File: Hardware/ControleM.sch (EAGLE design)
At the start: 17 parts, among them IC1 TL082P, IC2 TL082P, U1 LT1054CP

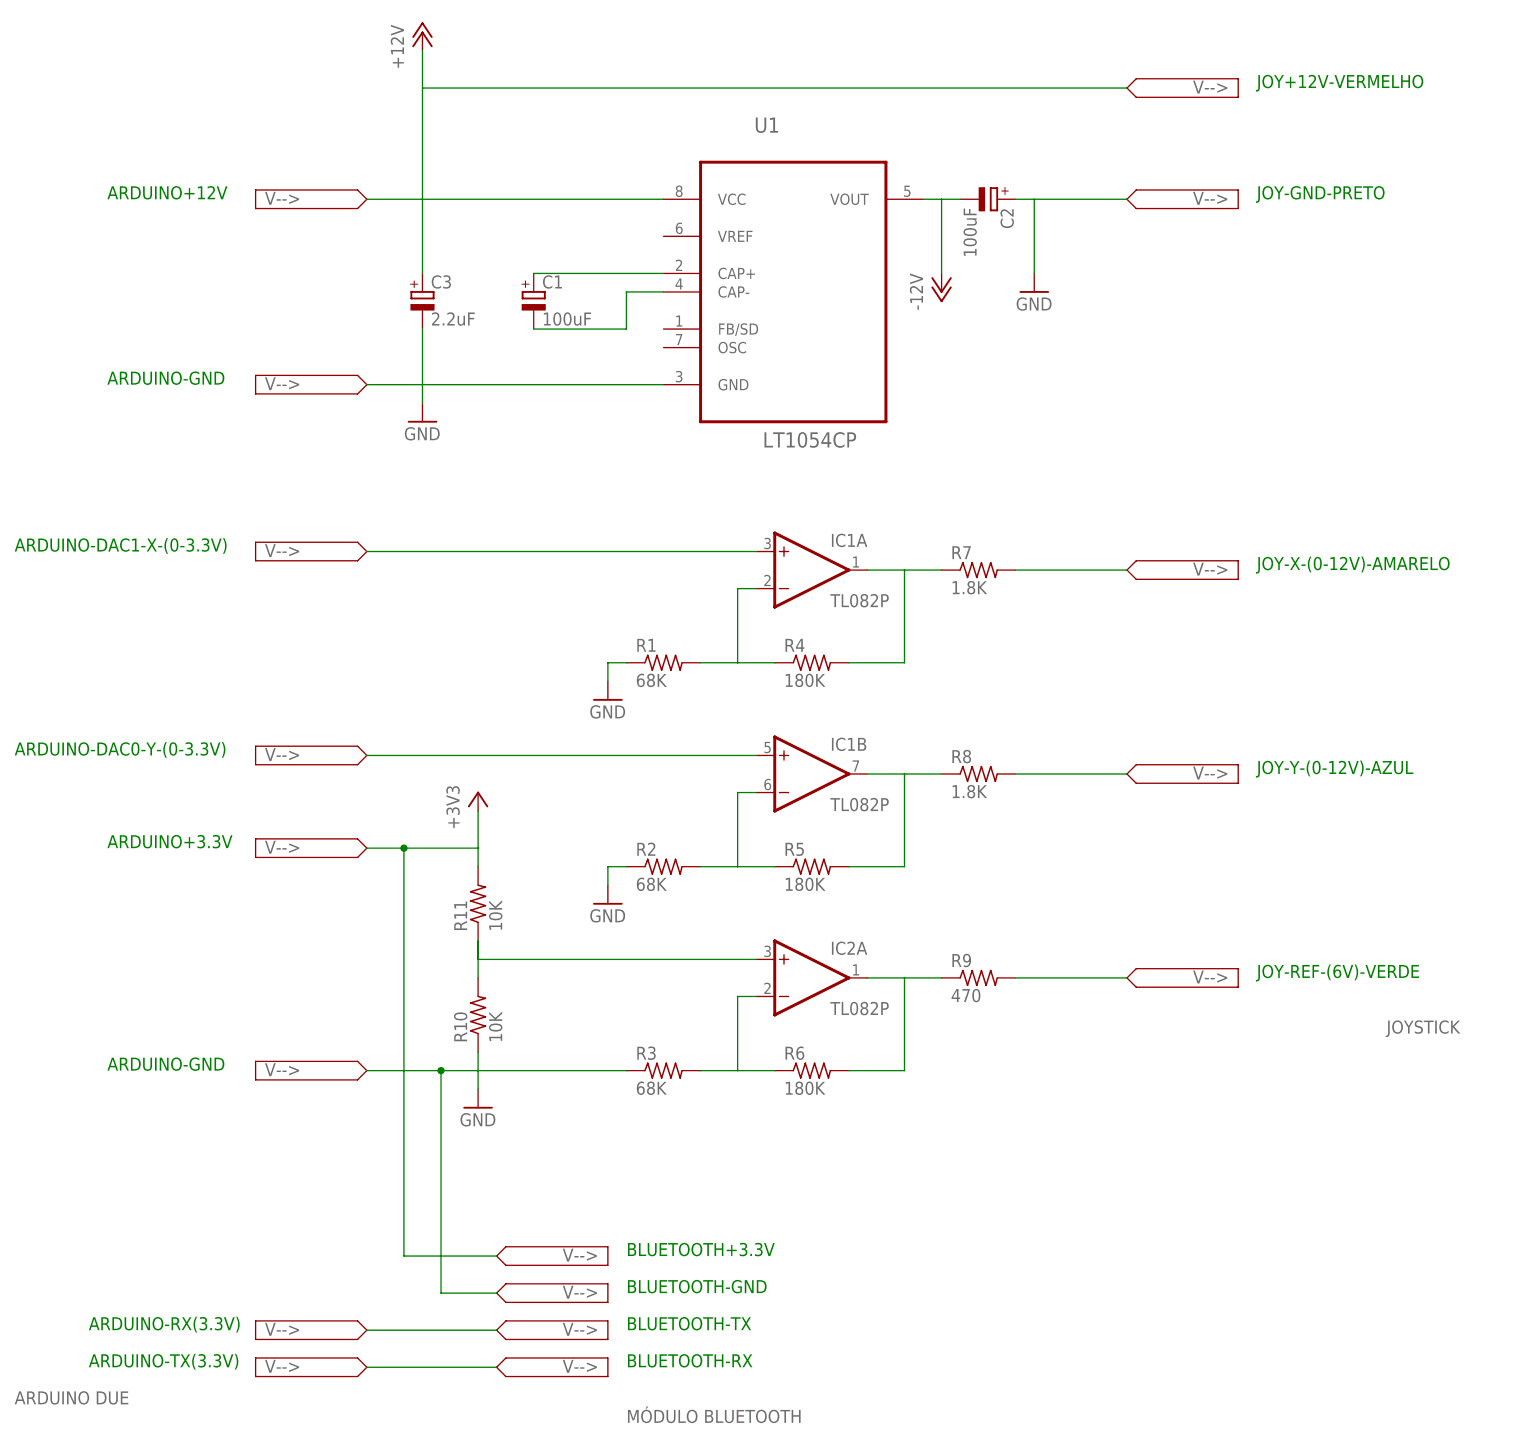
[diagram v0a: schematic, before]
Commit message: Correção do fundo de escala no DAC e REF retorno
A variação máxima do DAC foi ajustada para chegar em +ou-10% de VCC
sobre o meio da escala. Foi necessário devido a característica do DAC da
Arduino Due.

Outra alteração foi colher o sinal de REF (metade de 3,3v ) do divisor
de tensão e realimentar no Analog2 de maneira a garantir que o centro da
escala no DAC reflita a metade da tensão medida.
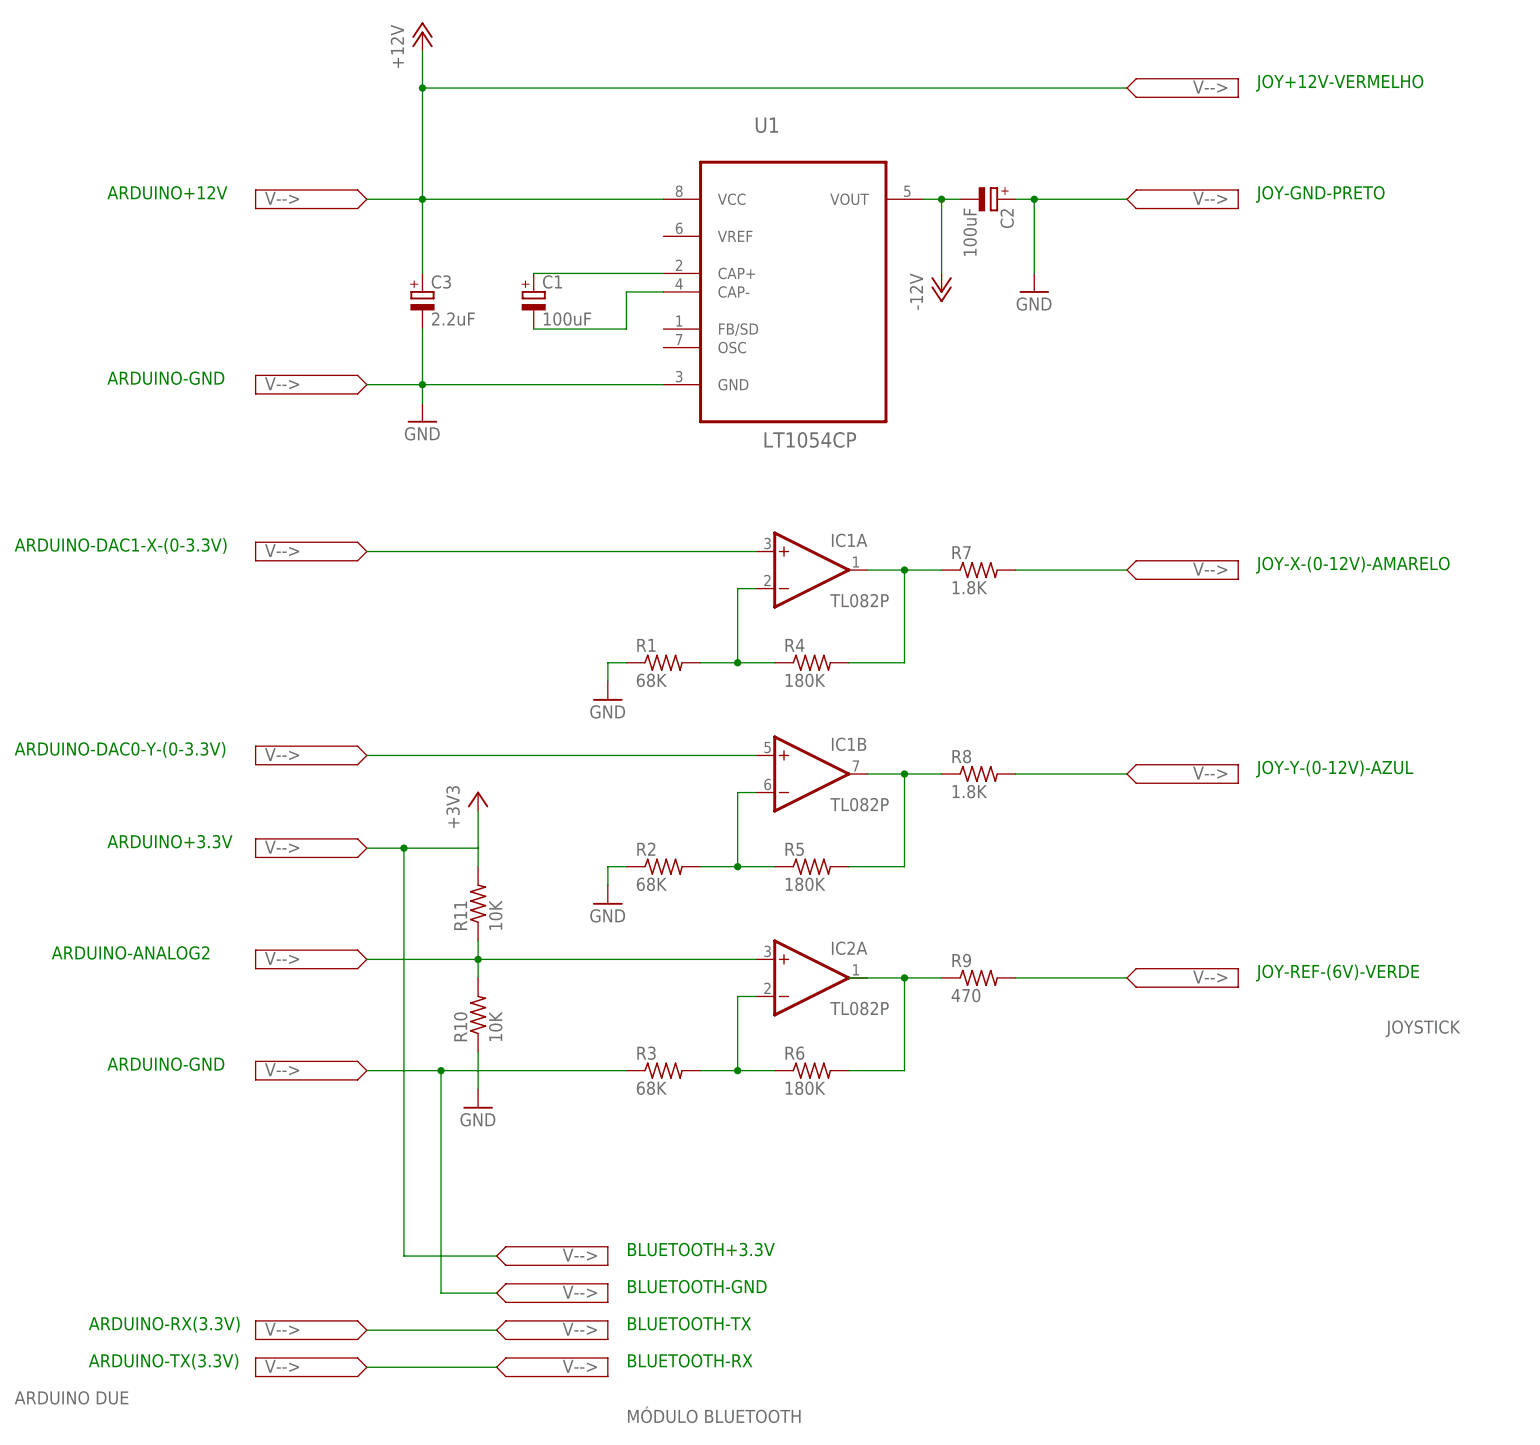
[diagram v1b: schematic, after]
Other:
- note added: "ARDUINO-ANALOG2"
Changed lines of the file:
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@@
 <part name="SUPPLY16" library="supply2" deviceset="V--&gt;" device=""/>
 <part name="SUPPLY17" library="supply2" deviceset="V--&gt;" device=""/>
+<part name="ARDUINO_ANALOG2" library="supply2" deviceset="V--&gt;" device=""/>
 </parts>
 <sheets>
@@
 <rectangle x1="154.94" y1="-55.88" x2="205.74" y2="78.74" layer="100"/>
 <text x="193.04" y="-53.34" size="1.778" layer="95">JOYSTICK</text>
+<text x="10.16" y="-43.18" size="1.778" layer="91">ARDUINO-ANALOG2</text>
 </plain>
 <instances>
@@
 <instance part="SUPPLY16" gate="G$1" x="172.72" y="60.96" rot="MR0"/>
 <instance part="SUPPLY17" gate="G$1" x="172.72" y="76.2" rot="MR0"/>
+<instance part="ARDUINO_ANALOG2" gate="G$1" x="38.1" y="-43.18"/>
 </instances>
 <busses>
@@
 <pinref part="GND1" gate="1" pin="GND"/>
 <wire x1="60.96" y1="35.56" x2="60.96" y2="33.02" width="0.1524" layer="91"/>
+<junction x="60.96" y="35.56"/>
 </segment>
 <segment>
@@
 <wire x1="144.78" y1="60.96" x2="144.78" y2="50.8" width="0.1524" layer="91"/>
 <wire x1="157.48" y1="60.96" x2="144.78" y2="60.96" width="0.1524" layer="91"/>
+<junction x="144.78" y="60.96"/>
 </segment>
 <segment>
@@
 <wire x1="60.96" y1="76.2" x2="60.96" y2="60.96" width="0.1524" layer="91"/>
 <wire x1="157.48" y1="76.2" x2="60.96" y2="76.2" width="0.1524" layer="91"/>
+<junction x="60.96" y="60.96"/>
+<junction x="60.96" y="76.2"/>
 </segment>
 </net>
@@
 <wire x1="106.68" y1="7.62" x2="104.14" y2="7.62" width="0.1524" layer="91"/>
 <wire x1="104.14" y1="7.62" x2="104.14" y2="-2.54" width="0.1524" layer="91"/>
+<junction x="104.14" y="-2.54"/>
 </segment>
 </net>
@@
 <wire x1="106.68" y1="-20.32" x2="104.14" y2="-20.32" width="0.1524" layer="91"/>
 <wire x1="104.14" y1="-20.32" x2="104.14" y2="-30.48" width="0.1524" layer="91"/>
+<junction x="104.14" y="-30.48"/>
 </segment>
 </net>
 <net name="N$7" class="0">
 <segment>
+<pinref part="IC2" gate="A" pin="OUT"/>
+<pinref part="R9" gate="G$1" pin="1"/>
+<wire x1="121.92" y1="-45.72" x2="127" y2="-45.72" width="0.1524" layer="91"/>
+<wire x1="132.08" y1="-45.72" x2="127" y2="-45.72" width="0.1524" layer="91"/>
 <pinref part="R6" gate="G$1" pin="2"/>
+<wire x1="121.92" y1="-45.72" x2="119.38" y2="-45.72" width="0.1524" layer="91"/>
 <wire x1="119.38" y1="-58.42" x2="127" y2="-58.42" width="0.1524" layer="91"/>
-<pinref part="R9" gate="G$1" pin="1"/>
-<pinref part="IC2" gate="A" pin="OUT"/>
-<wire x1="121.92" y1="-45.72" x2="127" y2="-45.72" width="0.1524" layer="91"/>
-<wire x1="127" y1="-45.72" x2="132.08" y2="-45.72" width="0.1524" layer="91"/>
 <wire x1="127" y1="-58.42" x2="127" y2="-45.72" width="0.1524" layer="91"/>
+<junction x="127" y="-45.72"/>
 </segment>
 </net>
@@
 <wire x1="127" y1="10.16" x2="132.08" y2="10.16" width="0.1524" layer="91"/>
 <wire x1="127" y1="-2.54" x2="127" y2="10.16" width="0.1524" layer="91"/>
+<junction x="127" y="10.16"/>
 </segment>
 </net>
@@
 <wire x1="127" y1="-17.78" x2="132.08" y2="-17.78" width="0.1524" layer="91"/>
 <wire x1="127" y1="-30.48" x2="127" y2="-17.78" width="0.1524" layer="91"/>
+<junction x="127" y="-17.78"/>
 </segment>
 </net>
@@
 <wire x1="106.68" y1="-48.26" x2="104.14" y2="-48.26" width="0.1524" layer="91"/>
 <wire x1="104.14" y1="-48.26" x2="104.14" y2="-58.42" width="0.1524" layer="91"/>
+<junction x="104.14" y="-58.42"/>
 </segment>
 </net>
@@
 <pinref part="R11" gate="G$1" pin="1"/>
 <pinref part="R10" gate="G$1" pin="2"/>
-<wire x1="68.58" y1="-40.64" x2="68.58" y2="-45.72" width="0.1524" layer="91"/>
 <pinref part="IC2" gate="A" pin="+IN"/>
+<wire x1="68.58" y1="-43.18" x2="68.58" y2="-45.72" width="0.1524" layer="91"/>
 <wire x1="106.68" y1="-43.18" x2="68.58" y2="-43.18" width="0.1524" layer="91"/>
 <wire x1="68.58" y1="-43.18" x2="68.58" y2="-40.64" width="0.1524" layer="91"/>
+<wire x1="68.58" y1="-43.18" x2="53.34" y2="-43.18" width="0.1524" layer="91"/>
+<junction x="68.58" y="-43.18"/>
 </segment>
 </net>
@@
 <wire x1="132.08" y1="60.96" x2="134.62" y2="60.96" width="0.1524" layer="91"/>
 <wire x1="132.08" y1="50.8" x2="132.08" y2="60.96" width="0.1524" layer="91"/>
-</segment>
-</net>
+<junction x="132.08" y="60.96"/>
+</segment>
+</net>
